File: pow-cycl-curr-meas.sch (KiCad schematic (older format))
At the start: 0 parts

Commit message: Power cycling module improvement
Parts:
- added Q? (x4): SQS401EN-T1_BE3, antmicro-footprints:Vishay_PowerPAK_1212-8_Single, symbol antmicroTransistorsFETsMOSFETsSingle:SQS401EN-T1_BE3
- added Q? (x4): SSM3K15ACT, antmicro-footprints:SSM3K15ACT, symbol antmicroTransistorsFETsMOSFETsSingle:SSM3K15ACT
- added R? (x4): R_10k_0402, antmicro-footprints:0402-res, symbol antmicroResistors0402:R_10k_0402
- added R? (x4): R_4k7_0402, antmicro-footprints:0402-res, symbol antmicroResistors0402:R_4k7_0402
- added U?: TCA9537, antmicro-footprints:VSSOP(10), symbol antmicroInterfaceIOExpanders:TCA9537
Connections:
- net labels added: GND, NUC_1, NUC_2, NUC_3, NUC_4, PC_1, PC_2, PC_3, PC_4, VCC12V0
- wire segments 0 -> 52
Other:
- note added: "Switching Blocks"

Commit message: Power cycling module update
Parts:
- removed U?: TCA9537, antmicro-footprints:VSSOP(10), symbol antmicroInterfaceIOExpanders:TCA9537
- added Q?: SQS401EN-T1_BE3, antmicro-footprints:Vishay_PowerPAK_1212-8_Single, symbol antmicroTransistorsFETsMOSFETsSingle:SQS401EN-T1_BE3
- added Q?: SSM3K15ACT, antmicro-footprints:SSM3K15ACT, symbol antmicroTransistorsFETsMOSFETsSingle:SSM3K15ACT
- added R?: R_10k_0402, antmicro-footprints:0402-res, symbol antmicroResistors0402:R_10k_0402
- added R? (x2): R_4k7_0402, antmicro-footprints:0402-res, symbol antmicroResistors0402:R_4k7_0402
- added R? (x6): R_0R_0402, antmicro-footprints:0402-res, symbol antmicroResistors0402:R_0R_0402
- added U?: TCA9534, symbol Interface_Expansion:TCA9534
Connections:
- net labels added: NUC_5, PC_5, SCL, SDA, VCC3V3
- wire segments 52 -> 92
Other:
- note added: "GPIO EXPANDER"
- note added: "Not used pins PX MUST be configured as outputs!\n"
- note added: "SWITCHING BLOCKS"
- note removed: "Switching Blocks"
- moved on the sheet: Q?, R?

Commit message: Power cycling module update
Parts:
- removed R? (x5): R_10k_0402, antmicro-footprints:0402-res, symbol antmicroResistors0402:R_10k_0402
- added C? (x2): C_100n_0402, antmicro-footprints:0402-cap, symbol antmicroCapacitors0402:C_100n_0402
- added C?: C_1u_0402, antmicro-footprints:0402-cap, symbol antmicroCapacitors0402:C_1u_0402
- added R? (x4): R_0R_0402, antmicro-footprints:0402-res, symbol antmicroResistors0402:R_0R_0402
- added R? (x5): R_10k_0402, antmicro-footprints:0402-res, symbol antmicroResistors0402:R_10k_0402
- added U?: ADS7828, Package_SO:TSSOP-16_4.4x5mm_P0.65mm, symbol Analog_ADC:ADS7828
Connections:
- net GND: now also C?.2, C?.2, C?.2, R?.2, R?.2, U?.9 (GND)
- net PC_1: now also R?.2
- net PC_2: now also R?.2
- net PC_3: now also R?.2
- net PC_4: now also R?.2
- net PC_5: now also R?.2
- net SCL: now also U?.14 (SCL)
- net SDA: now also U?.15 (SDA)
- net NUC_1 renamed C_MEAS_1
- net NUC_2 renamed C_MEAS_2
- net NUC_3 renamed C_MEAS_3
- net NUC_4 renamed C_MEAS_4
- net NUC_5 renamed C_MEAS_5
- net VCC3V3 renamed VCC5V0
- net VCC5V0: now also C?.1, C?.1, C?.1, R?.1, R?.1, R?.1, R?.1, R?.1, R?.1, R?.1, U?.10 (REF), U?.16 (VDD)
- new net: R?.1, R?.2, U?.12 (A0)
- new net: R?.1, R?.2, U?.13 (A1)
- new net C_ADC1: U?.1 (CH0)
- new net C_ADC2: U?.2 (CH1)
- new net C_ADC3: U?.3 (CH2)
- new net C_ADC4: U?.4 (CH3)
- new net C_ADC5: U?.5 (CH4)
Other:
- note added: "Expander filtration"
- note added: "REF"
- note added: "Supply\n"
- moved on the sheet: Q?, R?

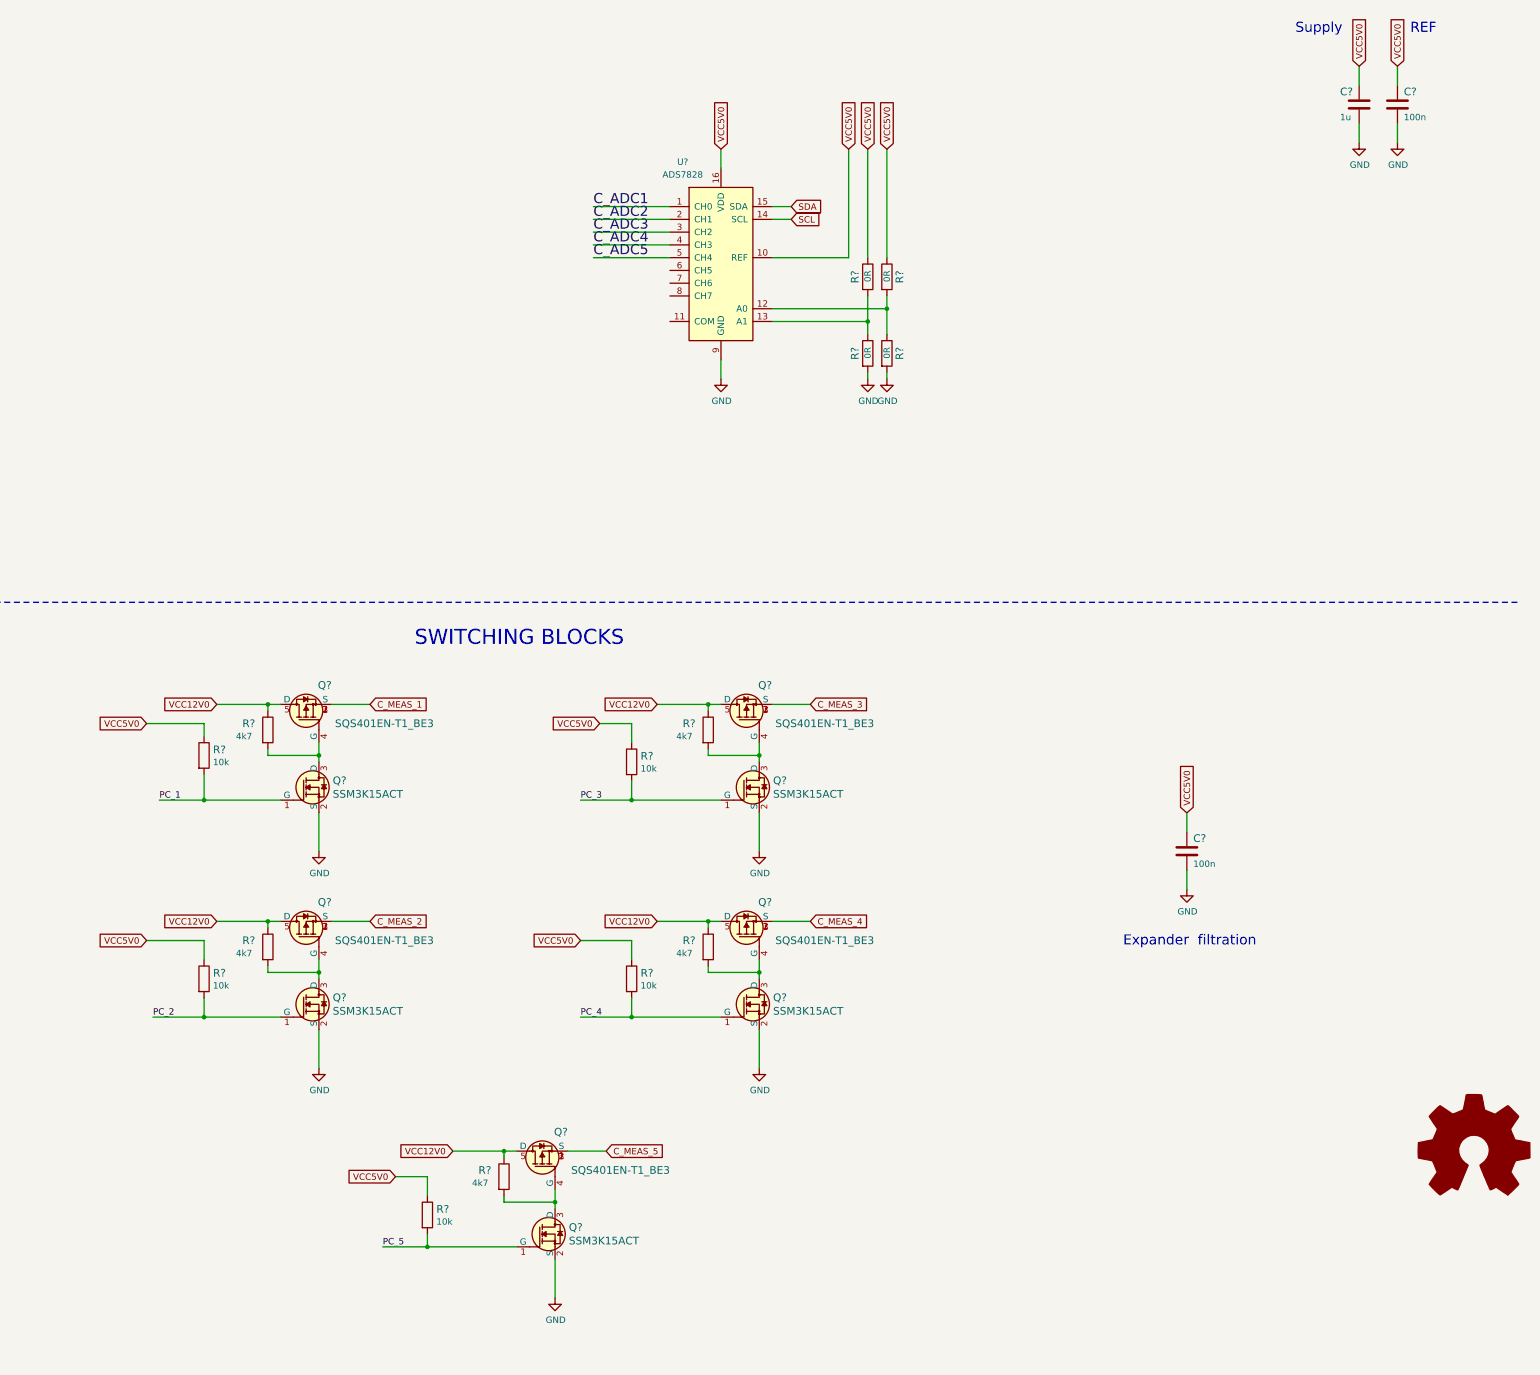
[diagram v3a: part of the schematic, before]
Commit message: Logic Shifter Module. Current Meas. implementation
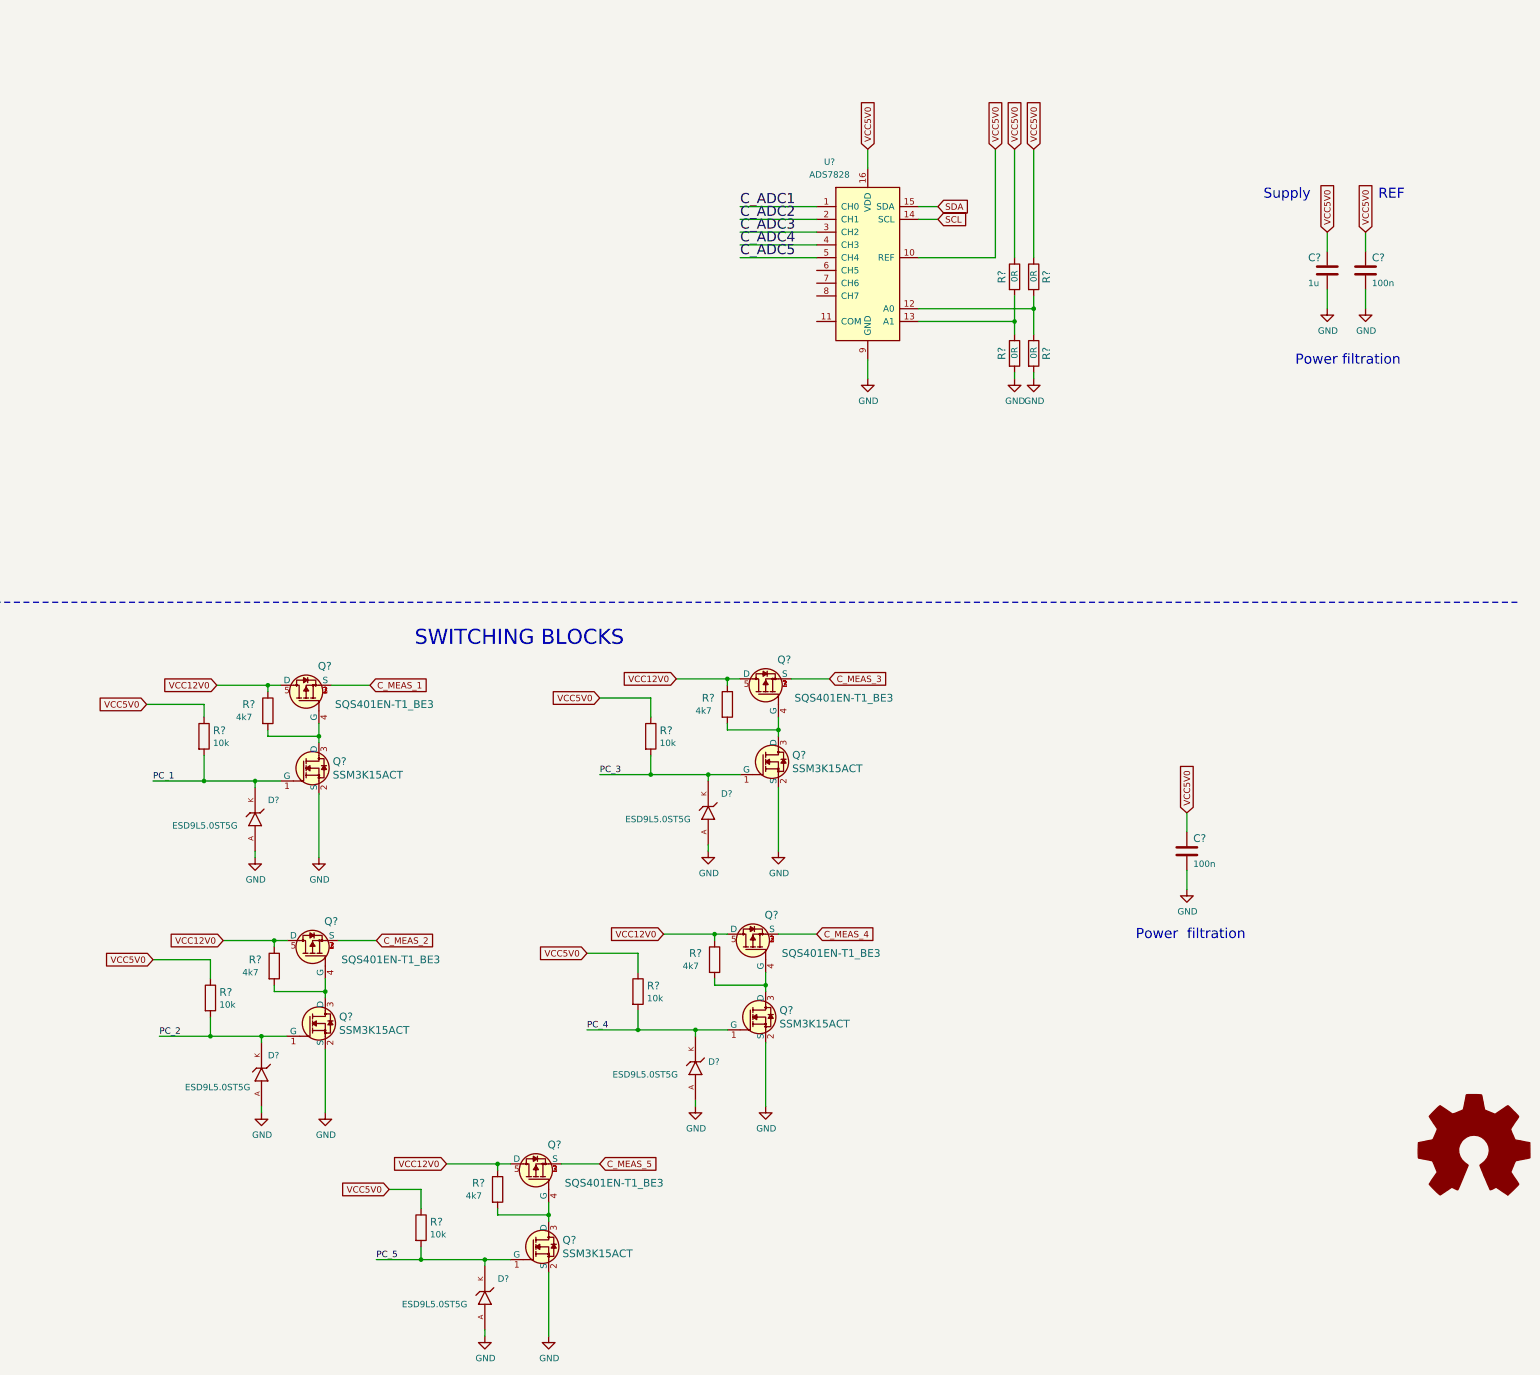
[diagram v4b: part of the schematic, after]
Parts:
- added D? (x5): ESD9L5.0ST5G, antmicro-footprints:DIOM1006X40N, symbol antmicroTVSDiodes:ESD9L5.0ST5G
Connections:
- net GND: now also D?.A, D?.A, D?.A, D?.A, D?.A
- net PC_1: now also D?.K
- net PC_2: now also D?.K
- net PC_3: now also D?.K
- net PC_4: now also D?.K
- net PC_5: now also D?.K
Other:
- note added: "Power filtration"
- note removed: "Expander filtration"
- moved on the sheet: C?, Q?, R?, U?

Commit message: Current Module upgrade. Logic unification.
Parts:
- removed D? (x5): ESD9L5.0ST5G, antmicro-footprints:DIOM1006X40N, symbol antmicroTVSDiodes:ESD9L5.0ST5G
- added U? (x5): TMCS1100A2-Q1, antmicro-footprints:SOIC-8_W3.9mm, symbol antmicroSensorsTransducersAccessories:TMCS1100A2-Q1
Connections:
- net C_ADC1: now also U?.7 (Vout)
- net C_ADC2: now also U?.7 (Vout)
- net C_ADC3: now also U?.7 (Vout)
- net C_ADC4: now also U?.7 (Vout)
- net C_ADC5: now also U?.7 (Vout)
- net C_MEAS_1: now also U?.1 (IN+), U?.2 (IN+)
- net C_MEAS_2: now also U?.1 (IN+), U?.2 (IN+)
- net C_MEAS_3: now also U?.1 (IN+), U?.2 (IN+)
- net C_MEAS_4: now also U?.1 (IN+), U?.2 (IN+)
- net C_MEAS_5: now also U?.1 (IN+), U?.2 (IN+)
- net GND: now also U?.5 (GND), U?.5 (GND), U?.5 (GND), U?.5 (GND), U?.5 (GND), U?.6 (Vref), U?.6 (Vref), U?.6 (Vref), U?.6 (Vref), U?.6 (Vref)
- net VCC5V0: no longer C?.1, C?.1, R?.1, R?.1, R?.1, R?.1, R?.1, R?.1, R?.1, R?.1, R?.1, R?.1, R?.1, U?.10 (REF), U?.16 (VDD), U?.16 (VDD)
- new net LOAD_1: U?.3 (IN-), U?.4 (IN-)
- new net LOAD_2: U?.3 (IN-), U?.4 (IN-)
- new net LOAD_3: U?.3 (IN-), U?.4 (IN-)
- new net LOAD_4: U?.3 (IN-), U?.4 (IN-)
- new net LOAD_5: U?.3 (IN-), U?.4 (IN-)
- new net VCC3V3: R?.1, R?.1, R?.1, R?.1, R?.1, R?.1, R?.1, R?.1, R?.1, R?.1, R?.1, U?.10 (REF), U?.16 (VDD), U?.16 (VDD), U?.8 (Vcc), U?.8 (Vcc), U?.8 (Vcc), U?.8 (Vcc), U?.8 (Vcc)
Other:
- note added: "ADC"
- note added: "HALL SENSORS"
- note added: "UP TO 15A"
- moved on the sheet: C?, R?

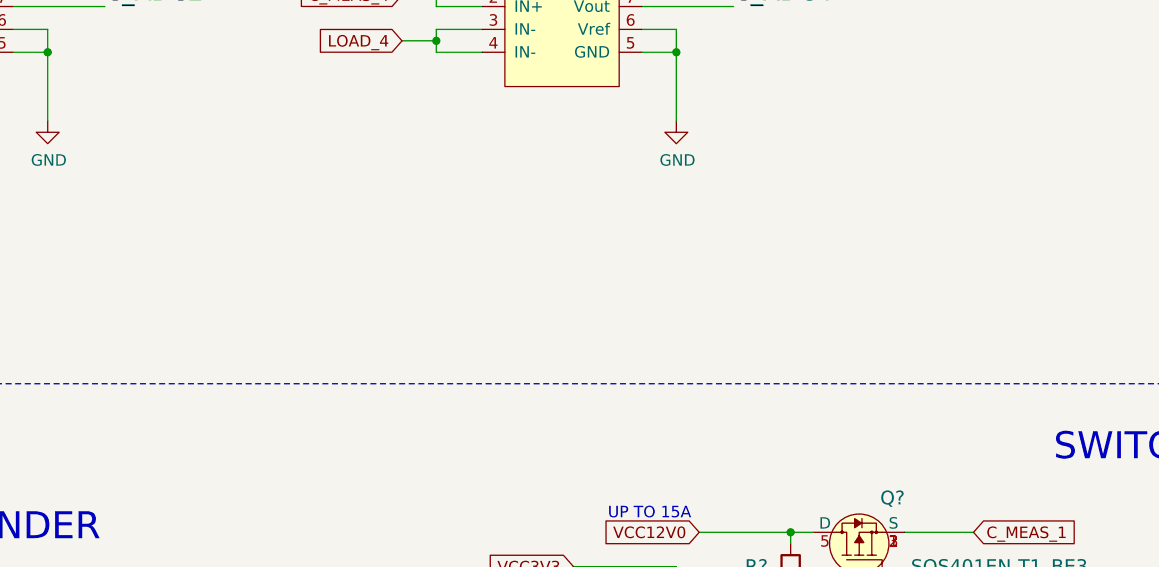
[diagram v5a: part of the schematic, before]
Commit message: Added connection between breakout boards
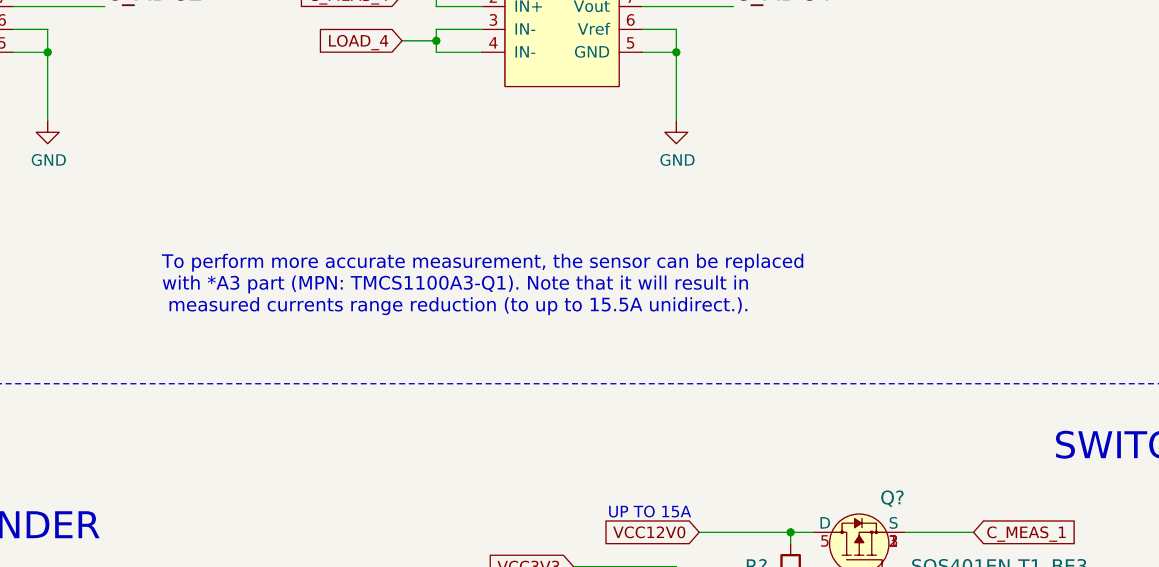
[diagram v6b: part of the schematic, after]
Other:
- note added: "To perform more accurate measurement, the sensor can be replaced\nwith *A3 part (MPN: TMCS1100A3-Q1). Note that it will result in\n measured currents range reduction (to up to 15.5A unidirect.)."
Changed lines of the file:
@@
 $Descr A3 16535 11693
 encoding utf-8
-Sheet 3 3
+Sheet 3 4
 Title "Power Cycling & Current Measurement Module"
 Date "2022-03-07"
@@
 Text Notes 11150 1050 0    118  ~ 0
 ADC
+Text Notes 3350 4950 0    59   ~ 0
+To perform more accurate measurement, the sensor can be replaced\nwith *A3 part (MPN: TMCS1100A3-Q1). Note that it will result in\n measured currents range reduction (to up to 15.5A unidirect.).
 $EndSCHEMATC

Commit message: Schematic improvements according to review's comments
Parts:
- U?: symbol Interface_Expansion:TCA9534 -> antmicroInterfaceIOExpanders:TCA9534; MPN (none) -> TCA9534ADWR; Manufaacturer (none) -> Texas Instruments
- U?: symbol Analog_ADC:ADS7828 -> antmicroDataAcquisitionAnalogtoDigitalConvertersADC:ADS7828; MPN (none) -> ADS7828E/250; Manufacturer (none) -> Texas Instruments
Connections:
- net VCC3V3: now also C?.1, C?.1
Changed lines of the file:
@@
 $EndComp
 $Comp
-L Interface_Expansion:TCA9534 U?
+L antmicroInterfaceIOExpanders:TCA9534 U?
 U 1 1 622B2CB2
 P 3300 7300
@@
 F 2 "" H 4250 6750 50  0001 C CNN
 F 3 "http://www.ti.com/lit/ds/symlink/tca9534.pdf" H 3400 7200 50  0001 C CNN
+F 4 "TCA9534ADWR" H 3300 7300 50  0001 C CNN "MPN"
+F 5 "Texas Instruments" H 3300 7300 50  0001 C CNN "Manufaacturer"
 	1    3300 7300
 	1    0    0    -1
@@
 SCL
 $Comp
-L Analog_ADC:ADS7828 U?
+L antmicroDataAcquisitionAnalogtoDigitalConvertersADC:ADS7828 U?
 U 1 1 6252165A
 P 10800 2550
@@
 F 2 "Package_SO:TSSOP-16_4.4x5mm_P0.65mm" H 11750 1850 50  0001 C CNN
 F 3 "http://www.ti.com/lit/ds/symlink/ads7828.pdf" H 10800 2550 50  0001 C CNN
+F 4 "ADS7828E/250 " H 10800 2550 50  0001 C CNN "MPN"
+F 5 "Texas Instruments" H 10800 2550 50  0001 C CNN "Manufacturer"
 	1    10800 2550
 	1    0    0    -1
@@
 Wire Wire Line
 	14900 2950 14900 2800
-Wire Wire Line
-	14100 2500 14100 2350
-Wire Wire Line
-	14900 2500 14900 2350
 $Comp
 L antmicroCapacitors0402:C_100n_0402 C?
@@
 Wire Wire Line
 	5650 8050 5650 8200
-Text Notes 14800 2100 0    79   ~ 0
+Text Notes 14800 1650 0    79   ~ 0
 REF
-Text Notes 13900 2100 0    79   ~ 0
+Text Notes 13950 1650 0    79   ~ 0
 Supply\n
 $Comp
@@
 Text Notes 11150 1050 0    118  ~ 0
 ADC
-Text Notes 3350 4950 0    59   ~ 0
+Text Notes 2050 4900 0    59   ~ 0
 To perform more accurate measurement, the sensor can be replaced\nwith *A3 part (MPN: TMCS1100A3-Q1). Note that it will result in\n measured currents range reduction (to up to 15.5A unidirect.).
+Text GLabel 14100 2200 1    50   Input ~ 0
+VCC3V3
+Text GLabel 14900 2200 1    50   Input ~ 0
+VCC3V3
+Wire Wire Line
+	14100 2200 14100 2500
+Wire Wire Line
+	14900 2200 14900 2500
 $EndSCHEMATC
